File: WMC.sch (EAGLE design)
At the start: 64 parts, among them IC5 MCP2551, IC6 MCP2515, IC7 ATMEGA32U4NT-TQFP, J1 LEFT MOTOR, J10 XT30F, J11 USB-B-PTH, J12 RoboClaw, J2 RIGHT MOTOR, J3 M01-2.5MM, J4 M01-2.5MM, J5 M01-2.5MM, J6 M01-2.5MM, J7 M01-2.5MM, J8 M01-2.5MM, J9 XT30F, Q1 NTD5867NLT4G, Q2 NTD5867NLT4G

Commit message: Routing, ERC, DRC for v1.0 release
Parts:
- D2, D3: value (none) -> SS56
- D4, D5: value (none) -> 1N4148
- LED1, LED2: value (none) -> RED
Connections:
- net 5V: now also U$6.2
- net USB+: no longer U$6.2
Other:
- note added: "(C)2019 SuperHouse Automation: www.superhouse.tv"
- note added: "5V power is supplied by the RoboClaw via the comms header. ICSP VIN linked to RoboClaw 5V Fabricate with 2oz copper to provide adequate current capacity for high power tracks."
- note added: "SKU: WMC"
- note added: "To Do: * Sub-board to jumper to RoboClaw (or use IDC cable)"
- note added: "V1 (2019-10-22)"
- note added: "Wheelchair Motor Controller with CAN Bus Interface"
- note added: "www.superhouse.tv/wmc"
- note removed: "(C)2018-2019 SuperHouse Automation: www.superhouse.tv"
- note removed: "5V power is supplied by the RoboClaw via the comms header. USB VIN and ICSP VIN are linked. Fabricate with 2oz copper to provide adequate current capacity for high power tracks."
- note removed: "SKU: FSI6CAN"
- note removed: "To Do: * Sub-board to jumper to RoboClaw"
- note removed: "V2.1 (2019-05-10)"
- note removed: "Wheelchair Motor Controller CAN Bus Interface"
- note removed: "www.superhouse.tv/fsi6can"
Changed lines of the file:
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@@
 <part name="R1" library="SuperHouse-DiscreteSemi" library_urn="urn:adsk.eagle:library:11768461" deviceset="RESISTOR" device="0603" package3d_urn="urn:adsk.eagle:package:11768543/2" value="1K"/>
 <part name="R3" library="SuperHouse-DiscreteSemi" library_urn="urn:adsk.eagle:library:11768461" deviceset="RESISTOR" device="0603" package3d_urn="urn:adsk.eagle:package:11768543/2" value="1K"/>
-<part name="D2" library="SuperHouse-DiscreteSemi" library_urn="urn:adsk.eagle:library:11768461" deviceset="DIODE" device="SMA" package3d_urn="urn:adsk.eagle:package:7066222/3"/>
-<part name="D3" library="SuperHouse-DiscreteSemi" library_urn="urn:adsk.eagle:library:11768461" deviceset="DIODE" device="SMA" package3d_urn="urn:adsk.eagle:package:7066222/3"/>
+<part name="D2" library="SuperHouse-DiscreteSemi" library_urn="urn:adsk.eagle:library:11768461" deviceset="DIODE" device="SMA" package3d_urn="urn:adsk.eagle:package:7066222/3" value="SS56"/>
+<part name="D3" library="SuperHouse-DiscreteSemi" library_urn="urn:adsk.eagle:library:11768461" deviceset="DIODE" device="SMA" package3d_urn="urn:adsk.eagle:package:7066222/3" value="SS56"/>
 <part name="GND1" library="SuperHouse-SupplySymbols" library_urn="urn:adsk.eagle:library:11790503" deviceset="GND" device=""/>
 <part name="GND2" library="SuperHouse-SupplySymbols" library_urn="urn:adsk.eagle:library:11790503" deviceset="GND" device=""/>
@@
 <part name="R5" library="SuperHouse-DiscreteSemi" library_urn="urn:adsk.eagle:library:11768461" deviceset="RESISTOR" device="0603" package3d_urn="urn:adsk.eagle:package:11768543/2" value="10K"/>
 <part name="U$4" library="SuperHouse-SupplySymbols" library_urn="urn:adsk.eagle:library:11790503" deviceset="5V" device=""/>
-<part name="D4" library="SuperHouse-DiscreteSemi" library_urn="urn:adsk.eagle:library:11768461" deviceset="DIODE" device="SOD" package3d_urn="urn:adsk.eagle:package:7066224/2"/>
+<part name="D4" library="SuperHouse-DiscreteSemi" library_urn="urn:adsk.eagle:library:11768461" deviceset="DIODE" device="SOD" package3d_urn="urn:adsk.eagle:package:7066224/2" value="1N4148"/>
 <part name="R6" library="SuperHouse-DiscreteSemi" library_urn="urn:adsk.eagle:library:11768461" deviceset="RESISTOR" device="0603" package3d_urn="urn:adsk.eagle:package:11768543/2" value="1K"/>
-<part name="D5" library="SuperHouse-DiscreteSemi" library_urn="urn:adsk.eagle:library:11768461" deviceset="DIODE" device="SOD" package3d_urn="urn:adsk.eagle:package:7066224/2"/>
+<part name="D5" library="SuperHouse-DiscreteSemi" library_urn="urn:adsk.eagle:library:11768461" deviceset="DIODE" device="SOD" package3d_urn="urn:adsk.eagle:package:7066224/2" value="1N4148"/>
 <part name="R7" library="SuperHouse-DiscreteSemi" library_urn="urn:adsk.eagle:library:11768461" deviceset="RESISTOR" device="0603" package3d_urn="urn:adsk.eagle:package:11768543/2" value="10K"/>
 <part name="R8" library="SuperHouse-DiscreteSemi" library_urn="urn:adsk.eagle:library:11768461" deviceset="RESISTOR" device="0603" package3d_urn="urn:adsk.eagle:package:11768543/2" value="1K"/>
@@
 <part name="JP1" library="SuperHouse-Connectors" library_urn="urn:adsk.eagle:library:11765989" deviceset="M04" device="-PIN" package3d_urn="urn:adsk.eagle:package:11818439/2" value="CAN"/>
 <part name="U$6" library="SuperHouse-Connectors" library_urn="urn:adsk.eagle:library:11765989" deviceset="ICSP" device="-PIN" package3d_urn="urn:adsk.eagle:package:11765966/8"/>
-<part name="LED1" library="SuperHouse-LEDs" library_urn="urn:adsk.eagle:library:11790571" deviceset="LED" device="0603" package3d_urn="urn:adsk.eagle:package:7066240/3"/>
+<part name="LED1" library="SuperHouse-LEDs" library_urn="urn:adsk.eagle:library:11790571" deviceset="LED" device="0603" package3d_urn="urn:adsk.eagle:package:7066240/3" value="RED"/>
 <part name="GND6" library="SuperHouse-SupplySymbols" library_urn="urn:adsk.eagle:library:11790503" deviceset="GND" device=""/>
 <part name="GND5" library="SuperHouse-SupplySymbols" library_urn="urn:adsk.eagle:library:11790503" deviceset="GND" device=""/>
-<part name="LED2" library="SuperHouse-LEDs" library_urn="urn:adsk.eagle:library:11790571" deviceset="LED" device="0603" package3d_urn="urn:adsk.eagle:package:7066240/3"/>
+<part name="LED2" library="SuperHouse-LEDs" library_urn="urn:adsk.eagle:library:11790571" deviceset="LED" device="0603" package3d_urn="urn:adsk.eagle:package:7066240/3" value="RED"/>
+<part name="U$7" library="SuperHouse-SupplySymbols" library_urn="urn:adsk.eagle:library:11790503" deviceset="5V" device=""/>
 </parts>
 <sheets>
@@
 <plain>
 <frame x1="0" y1="0" x2="248.92" y2="185.42" columns="8" rows="5" layer="94"/>
-<text x="7.62" y="20.32" size="3.048" layer="94">Wheelchair Motor Controller CAN Bus Interface</text>
-<text x="38.1" y="14.478" size="1.778" layer="94">V2.1 (2019-05-10)</text>
-<text x="7.62" y="14.478" size="1.778" layer="94">SKU: FSI6CAN</text>
-<text x="7.366" y="9.398" size="1.778" layer="94">(C)2018-2019 SuperHouse Automation: www.superhouse.tv</text>
+<text x="7.62" y="20.32" size="3.048" layer="94">Wheelchair Motor Controller with CAN Bus Interface</text>
+<text x="38.1" y="14.478" size="1.778" layer="94">V1 (2019-10-22)</text>
+<text x="7.62" y="14.478" size="1.778" layer="94">SKU: WMC</text>
+<text x="7.366" y="9.398" size="1.778" layer="94">(C)2019 SuperHouse Automation: www.superhouse.tv</text>
 <text x="7.366" y="6.35" size="1.778" layer="94">Licensed under the TAPR Open Hardware License: www.tapr.org/ohl</text>
-<text x="68.326" y="14.478" size="1.778" layer="94">www.superhouse.tv/fsi6can</text>
+<text x="68.326" y="14.478" size="1.778" layer="94">www.superhouse.tv/wmc</text>
 <frame x1="5.08" y1="12.7" x2="109.22" y2="25.4" columns="0" rows="0" layer="94" border-left="no" border-top="no" border-right="no" border-bottom="no"/>
 <frame x1="5.08" y1="12.7" x2="35.56" y2="17.78" columns="8" rows="5" layer="94"/>
 <frame x1="35.56" y1="12.7" x2="66.04" y2="17.78" columns="8" rows="5" layer="94"/>
 <frame x1="5.08" y1="5.08" x2="109.22" y2="17.78" columns="0" rows="0" layer="94" border-left="no" border-top="no" border-right="no" border-bottom="no"/>
-<text x="137.16" y="30.48" size="1.778" layer="97">To Do:
-* Sub-board to jumper to RoboClaw</text>
+<text x="111.76" y="22.86" size="1.778" layer="97">To Do:
+* Sub-board to jumper to RoboClaw (or use IDC cable)</text>
 <wire x1="63.5" y1="66.04" x2="63.5" y2="33.02" width="0.4064" layer="97" style="longdash"/>
 <wire x1="10.16" y1="175.26" x2="170.18" y2="175.26" width="0.4064" layer="97" style="longdash"/>
@@
 <wire x1="129.54" y1="66.04" x2="129.54" y2="33.02" width="0.4064" layer="97" style="longdash"/>
 <text x="111.76" y="7.62" size="2.54" layer="97">5V power is supplied by the RoboClaw via the comms header.
-USB VIN and ICSP VIN are linked.
+ICSP VIN linked to RoboClaw 5V
 Fabricate with 2oz copper to provide adequate current capacity for high power tracks.</text>
 <text x="195.58" y="30.48" size="1.778" layer="97">D0:
@@
 <attribute name="NAME" x="30.48" y="53.975" size="1.778" layer="95"/>
 <attribute name="VALUE" x="30.48" y="40.64" size="1.778" layer="96"/>
+</instance>
+<instance part="U$7" gate="G$1" x="50.8" y="53.34" smashed="yes">
+<attribute name="VALUE" x="49.784" y="56.896" size="1.778" layer="96"/>
 </instance>
 </instances>
@@
 <wire x1="109.22" y1="48.26" x2="109.22" y2="53.34" width="0.1524" layer="91"/>
 </segment>
+<segment>
+<pinref part="U$6" gate="G$1" pin="2"/>
+<wire x1="48.26" y1="50.8" x2="50.8" y2="50.8" width="0.1524" layer="91"/>
+<pinref part="U$7" gate="G$1" pin="5V"/>
+<wire x1="50.8" y1="50.8" x2="50.8" y2="53.34" width="0.1524" layer="91"/>
+</segment>
 </net>
 <net name="D-" class="0">
@@
 <wire x1="33.02" y1="139.7" x2="35.56" y2="139.7" width="0.1524" layer="91"/>
 <label x="35.56" y="139.7" size="1.27" layer="95" xref="yes"/>
-</segment>
-<segment>
-<wire x1="48.26" y1="50.8" x2="50.8" y2="50.8" width="0.1524" layer="91"/>
-<label x="50.8" y="50.8" size="1.27" layer="95" xref="yes"/>
-<pinref part="U$6" gate="G$1" pin="2"/>
 </segment>
 </net>
@@
 </instance>
 <instance part="Q1" gate="G$1" x="55.88" y="38.1" smashed="yes">
-<attribute name="NAME" x="50.8" y="43.18" size="1.778" layer="95"/>
-<attribute name="VALUE" x="45.72" y="40.64" size="1.778" layer="96"/>
+<attribute name="NAME" x="55.88" y="40.64" size="1.778" layer="95"/>
+<attribute name="VALUE" x="33.02" y="38.1" size="1.778" layer="96"/>
 </instance>
 <instance part="Q2" gate="G$1" x="121.92" y="38.1" smashed="yes">
-<attribute name="NAME" x="116.84" y="43.18" size="1.778" layer="95"/>
-<attribute name="VALUE" x="111.76" y="40.64" size="1.778" layer="96"/>
+<attribute name="NAME" x="121.92" y="40.64" size="1.778" layer="95"/>
+<attribute name="VALUE" x="99.06" y="38.1" size="1.778" layer="96"/>
 </instance>
 <instance part="R1" gate="G$1" x="45.72" y="22.86" smashed="yes" rot="R90">

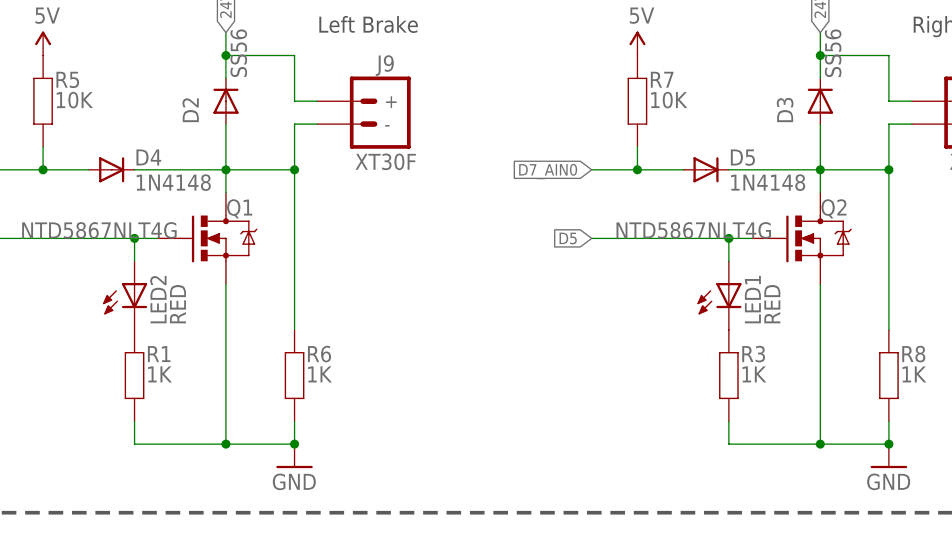
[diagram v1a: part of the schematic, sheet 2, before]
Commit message: Changed lock status LEDs to green to indicate chair will move when locks released - green means go
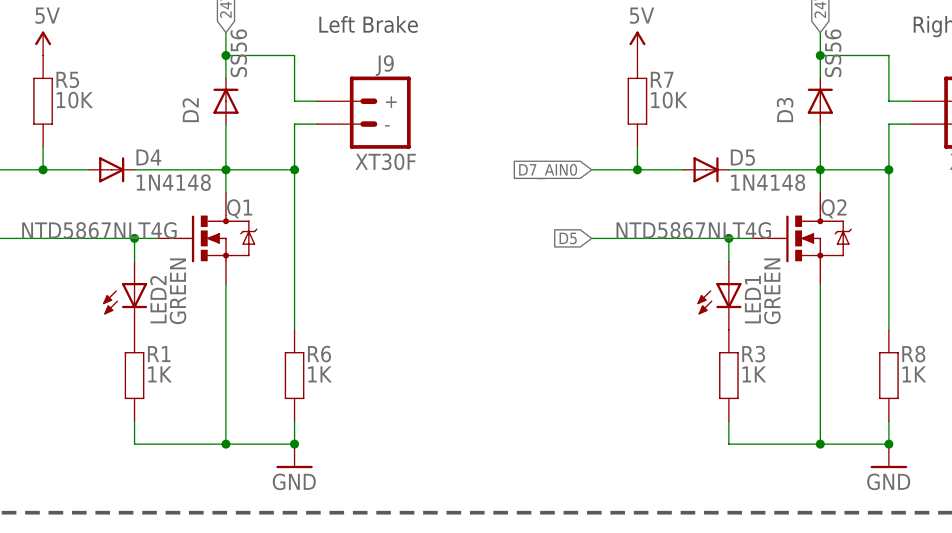
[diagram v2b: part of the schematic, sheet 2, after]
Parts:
- LED1, LED2: value RED -> GREEN
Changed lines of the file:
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@@
 <part name="JP1" library="SuperHouse-Connectors" library_urn="urn:adsk.eagle:library:11765989" deviceset="M04" device="-PIN" package3d_urn="urn:adsk.eagle:package:11818439/2" value="CAN"/>
 <part name="U$6" library="SuperHouse-Connectors" library_urn="urn:adsk.eagle:library:11765989" deviceset="ICSP" device="-PIN" package3d_urn="urn:adsk.eagle:package:11765966/8"/>
-<part name="LED1" library="SuperHouse-LEDs" library_urn="urn:adsk.eagle:library:11790571" deviceset="LED" device="0603" package3d_urn="urn:adsk.eagle:package:7066240/3" value="RED"/>
+<part name="LED1" library="SuperHouse-LEDs" library_urn="urn:adsk.eagle:library:11790571" deviceset="LED" device="0603" package3d_urn="urn:adsk.eagle:package:7066240/3" value="GREEN"/>
 <part name="GND6" library="SuperHouse-SupplySymbols" library_urn="urn:adsk.eagle:library:11790503" deviceset="GND" device=""/>
 <part name="GND5" library="SuperHouse-SupplySymbols" library_urn="urn:adsk.eagle:library:11790503" deviceset="GND" device=""/>
-<part name="LED2" library="SuperHouse-LEDs" library_urn="urn:adsk.eagle:library:11790571" deviceset="LED" device="0603" package3d_urn="urn:adsk.eagle:package:7066240/3" value="RED"/>
+<part name="LED2" library="SuperHouse-LEDs" library_urn="urn:adsk.eagle:library:11790571" deviceset="LED" device="0603" package3d_urn="urn:adsk.eagle:package:7066240/3" value="GREEN"/>
 <part name="U$7" library="SuperHouse-SupplySymbols" library_urn="urn:adsk.eagle:library:11790503" deviceset="5V" device=""/>
 </parts>
